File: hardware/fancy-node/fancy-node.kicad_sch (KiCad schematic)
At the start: 63 parts, among them J1 USB_B_Micro, J2 Conn_01x06, J3 Conn_01x03, J4 Conn_01x03, J5 Conn_01x04, J6 Conn_01x02, SW1 SW_Push, SW2 SW_Push, SW3 SW_Push, SW4 SW_SPDT, U1 CH340X, U2 STM32G030C8T6, U3 WS2812b, U4 HT75xx-1-SOT89, U5 RFM69CW-915MHZ, U6 TP4056

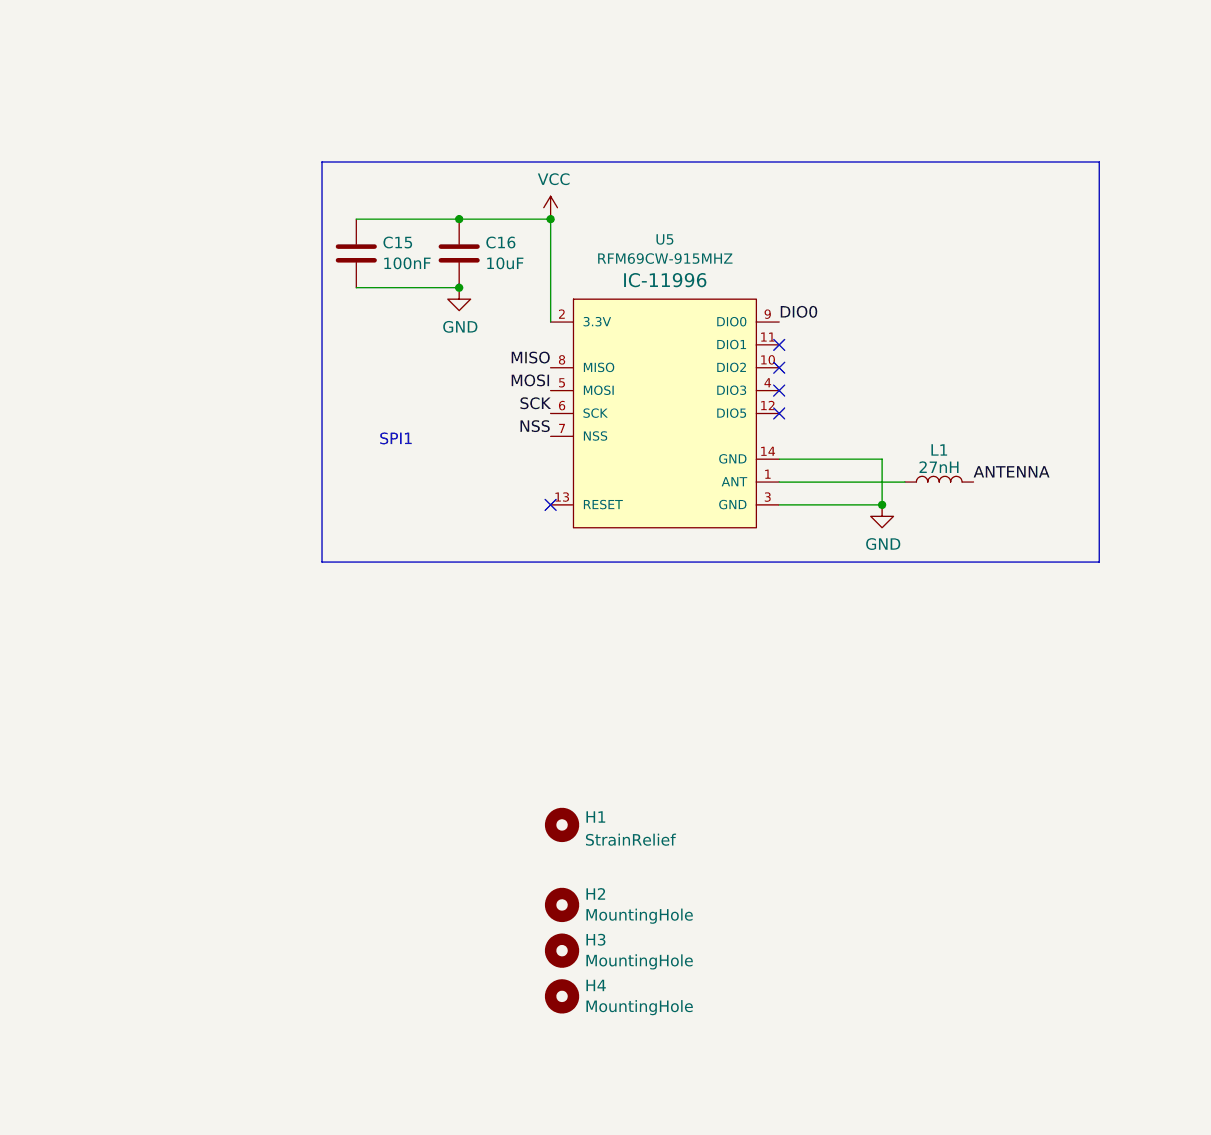
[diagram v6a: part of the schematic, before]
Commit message: Complete routing for fancy-node v1.2
Change-Id: I592d8a70fb0dd3ce7e678b66b73a8dfb2f1c9b60
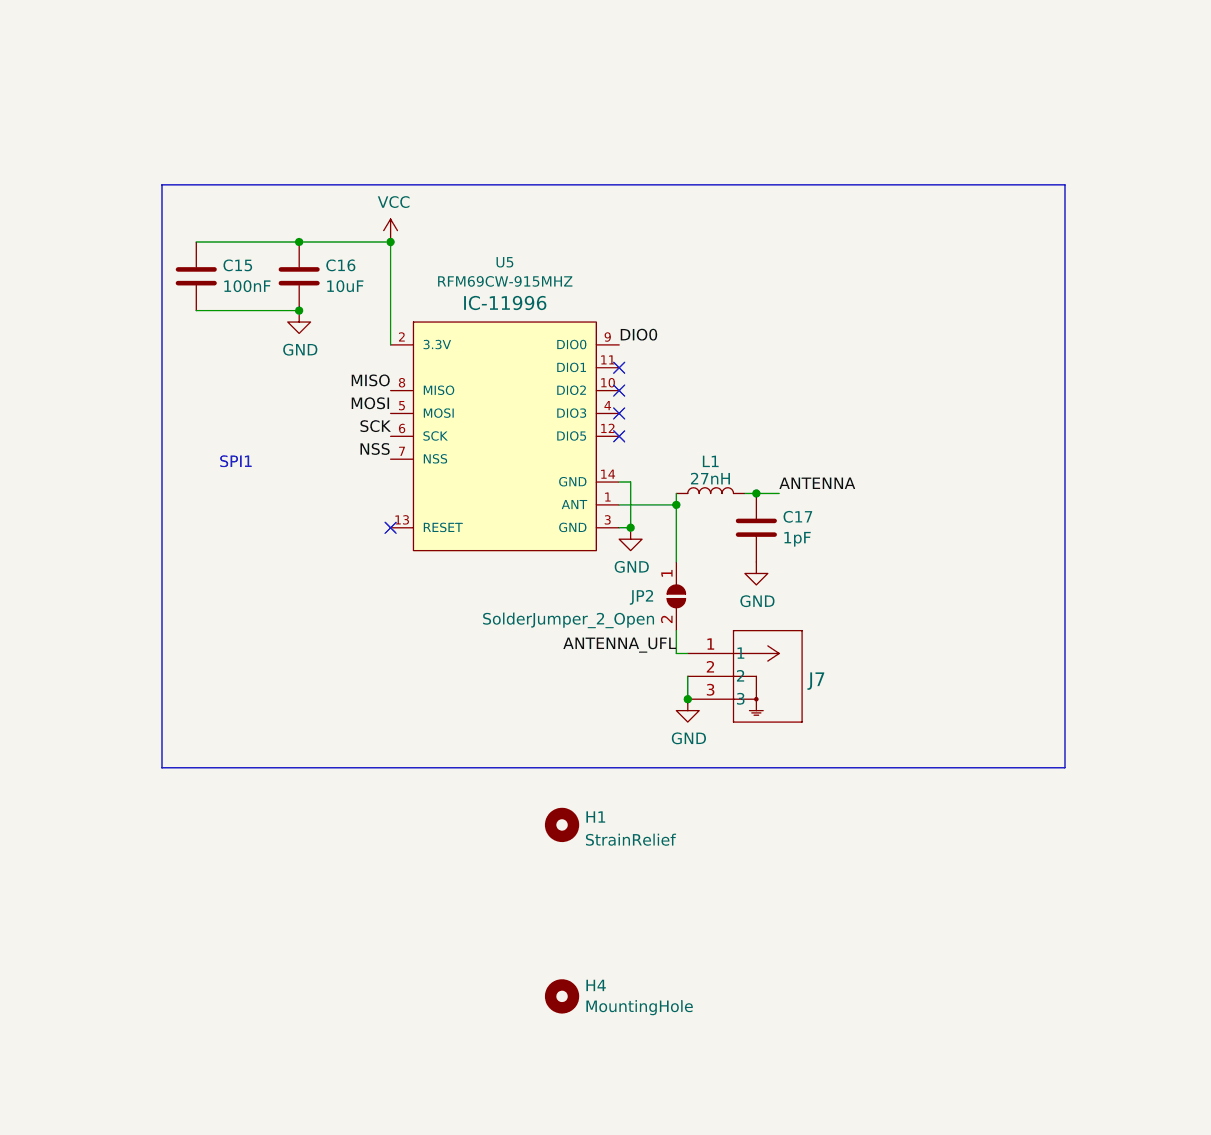
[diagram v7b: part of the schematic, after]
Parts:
- removed H2, H3: MountingHole, MountingHole:MountingHole_3.2mm_M3, symbol Mechanical:MountingHole
- added C17: 1pF, Capacitor_SMD:C_0402_1005Metric_Pad0.74x0.62mm_HandSolder, symbol Device:C
- added J7: 2337019-1, Homebrew:CONN_2337019-1, symbol Homebrew:TE_U.FL_MALE_SMT
- added JP2: SolderJumper_2_Open, Jumper:SolderJumper-2_P1.3mm_Open_TrianglePad1.0x1.5mm, symbol Jumper:SolderJumper_2_Open
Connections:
- net ANTENNA: now also C17.1
- net GND: now also C17.2, J7.2, J7.3
- net at L1.1, U5.1 (ANT): now also JP2.1 (A)
- new net ANTENNA_UFL: J7.1, JP2.2 (B)
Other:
- moved on the sheet: C15, C16, L1, U5

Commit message: Generate fab files for fancy-node v1.2
Change-Id: If2130e4a93829307ed5471cd4c6d67e4a752f069
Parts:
- C9: value 10uF -> 100nF; footprint Capacitor_SMD:C_0603_1608Metric -> Capacitor_SMD:C_0402_1005Metric_Pad0.74x0.62mm_HandSolder; LCSC C96446 -> C307331
- SW1, SW2, SW3: LCSC C318884 -> C498310
- U3: footprint LED_SMD:LED_WS2812B_PLCC4_5.0x5.0mm_P3.2mm -> Homebrew:LED_XINGLIGHT_WS2812B_PLCC4_5.0x5.0mm_P3.2mm; LCSC C2874885 -> C2843785
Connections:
- net GND: now also C9.2; no longer C9.1
- net VBATT_DIV: now also C9.1; no longer C9.2
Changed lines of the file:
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@@
-    )
-  )
-  (symbol (lib_id "Device:C") (at 262.89 63.5 180) (unit 1)
-    (in_bom yes) (on_board yes) (dnp no)
-    (property "Reference" "C9" (at 265.811 62.3316 0)
-      (effects (font (size 1.27 1.27)) (justify right))
-    )
-    (property "Value" "10uF" (at 265.811 64.643 0)
-      (effects (font (size 1.27 1.27)) (justify right))
-    )
-    (property "Footprint" "Capacitor_SMD:C_0603_1608Metric" (at 261.9248 59.69 0)
-      (effects (font (size 1.27 1.27)) hide)
-    )
-    (property "Datasheet" "~" (at 262.89 63.5 0)
-      (effects (font (size 1.27 1.27)) hide)
-    )
-    (property "LCSC" "C96446" (at 262.89 63.5 0)
-      (effects (font (size 1.27 1.27)) hide)
-    )
-    (pin "1")
-    (pin "2")
-    (instances
-      (project "fancy-node"
-        (path "/e443e095-f4ba-4771-8554-3425f127ef3e"
-          (reference "C9") (unit 1)
-        )
-      )
     )
   )
@@
       (effects (font (size 1.27 1.27)) hide)
     )
-    (property "LCSC" "C318884" (at 27.94 92.71 0)
+    (property "LCSC" "C498310" (at 27.94 92.71 0)
       (effects (font (size 1.27 1.27)) hide)
     )
@@
         (path "/e443e095-f4ba-4771-8554-3425f127ef3e"
           (reference "R16") (unit 1)
+        )
+      )
+    )
+  )
+  (symbol (lib_id "Device:C") (at 262.89 63.5 0) (unit 1)
+    (in_bom yes) (on_board yes) (dnp no)
+    (property "Reference" "C9" (at 265.811 62.3316 0)
+      (effects (font (size 1.27 1.27)) (justify left))
+    )
+    (property "Value" "100nF" (at 265.811 64.643 0)
+      (effects (font (size 1.27 1.27)) (justify left))
+    )
+    (property "Footprint" "Capacitor_SMD:C_0402_1005Metric_Pad0.74x0.62mm_HandSolder" (at 263.8552 67.31 0)
+      (effects (font (size 1.27 1.27)) hide)
+    )
+    (property "Datasheet" "~" (at 262.89 63.5 0)
+      (effects (font (size 1.27 1.27)) hide)
+    )
+    (property "LCSC" "C307331" (at 262.89 63.5 0)
+      (effects (font (size 1.27 1.27)) hide)
+    )
+    (pin "1")
+    (pin "2")
+    (instances
+      (project "fancy-node"
+        (path "/e443e095-f4ba-4771-8554-3425f127ef3e"
+          (reference "C9") (unit 1)
         )
       )
@@
       (effects (font (size 1.27 1.27)) hide)
     )
-    (property "LCSC" "C318884" (at 43.18 95.25 0)
+    (property "LCSC" "C498310" (at 43.18 95.25 0)
       (effects (font (size 1.27 1.27)) hide)
     )
@@
       (effects (font (size 1.524 1.524)))
     )
-    (property "Footprint" "LED_SMD:LED_WS2812B_PLCC4_5.0x5.0mm_P3.2mm" (at 240.03 222.25 0)
+    (property "Footprint" "Homebrew:LED_XINGLIGHT_WS2812B_PLCC4_5.0x5.0mm_P3.2mm" (at 240.03 222.25 0)
       (effects (font (size 1.524 1.524)) hide)
     )
@@
       (effects (font (size 1.524 1.524)) hide)
     )
-    (property "LCSC" "C2874885" (at 241.3 207.01 0)
+    (property "LCSC" "C2843785" (at 241.3 207.01 0)
       (effects (font (size 1.27 1.27)) hide)
     )
@@
       (effects (font (size 1.27 1.27)) hide)
     )
-    (property "LCSC" "C318884" (at 194.31 69.85 0)
-      (effects (font (size 1.27 1.27)) hide)
-    )
+    (property "LCSC" "C498310" (at 194.31 69.85 0)
+      (effects (font (size 1.27 1.27)) hide)
+    )
